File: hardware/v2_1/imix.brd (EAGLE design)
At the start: 62.2 x 101.6 mm, 143 parts, among them SW1 PTS645SM43SMTR92_LFS, SW2 PTS645SM43SMTR92_LFS, U1 74LVC4066BQ, U10 ISL29035, U11 FX0S8700CQ, U12 296-12686-1-ND, U13 74LVC4066BQ, U14 SIP32401A, U3 TLV3202, U4 LM358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

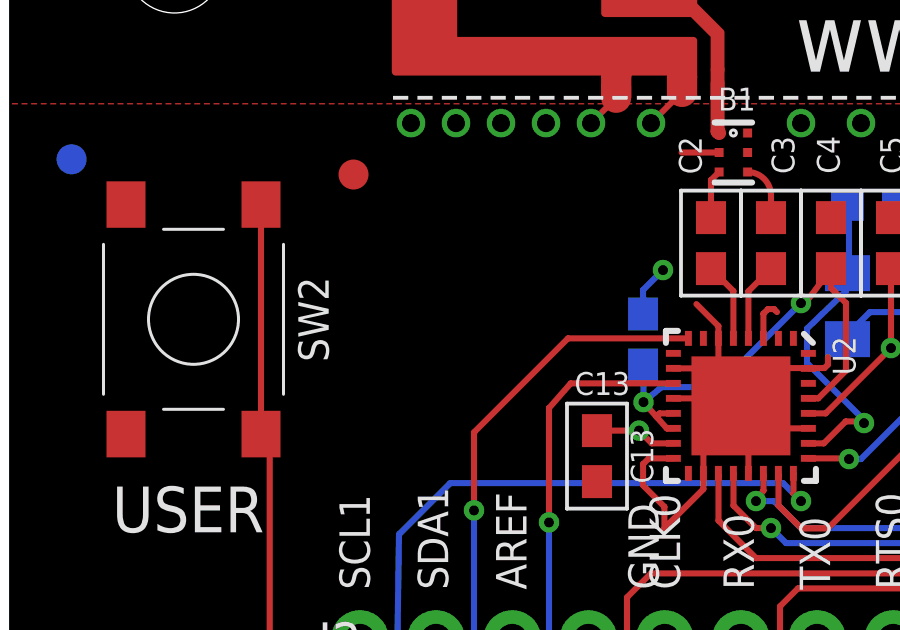
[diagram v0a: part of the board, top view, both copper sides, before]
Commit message: Add OSHW logo to silkscreen
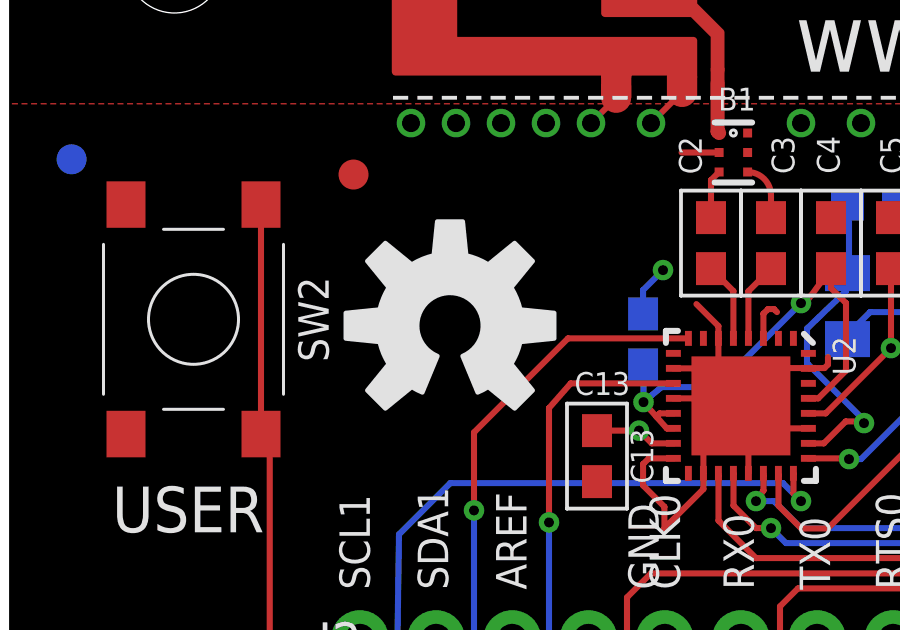
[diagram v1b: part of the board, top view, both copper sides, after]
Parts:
- added U$9: (no value), SparkFun-Aesthetics:OSHW-LOGO-L
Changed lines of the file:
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@@
 <element name="U$17" library="shaneleonard-master-lbr" package="FIDUCIAL" value="FIDUCIAL" x="59.944" y="10.414"/>
 <element name="U$18" library="shaneleonard-master-lbr" package="FIDUCIAL" value="FIDUCIAL" x="11.684" y="91.44"/>
+<element name="U$9" library="SparkFun-Aesthetics" package="OSHW-LOGO-L" value="" x="14.9" y="86.4"/>
 </elements>
 <signals>
